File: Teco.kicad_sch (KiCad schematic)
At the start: 56 parts, among them Q1 BC848, Q2 BC848, Q3 IRLML9303, SW1 BUTTON

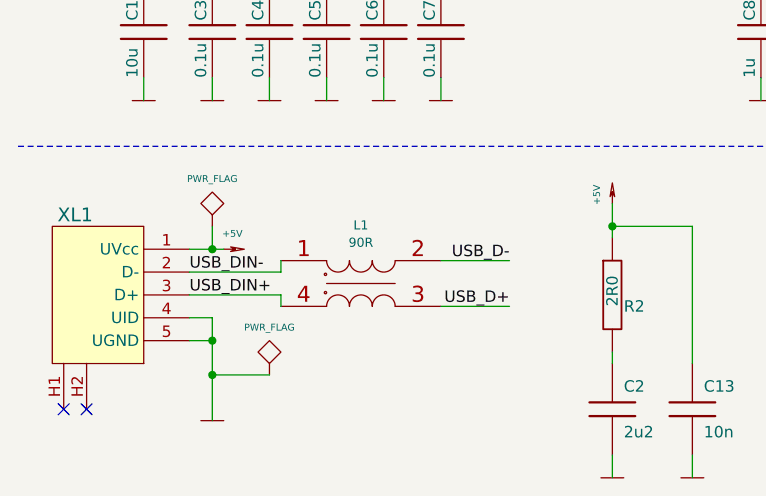
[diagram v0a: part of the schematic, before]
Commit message: switch to KiCAD 7
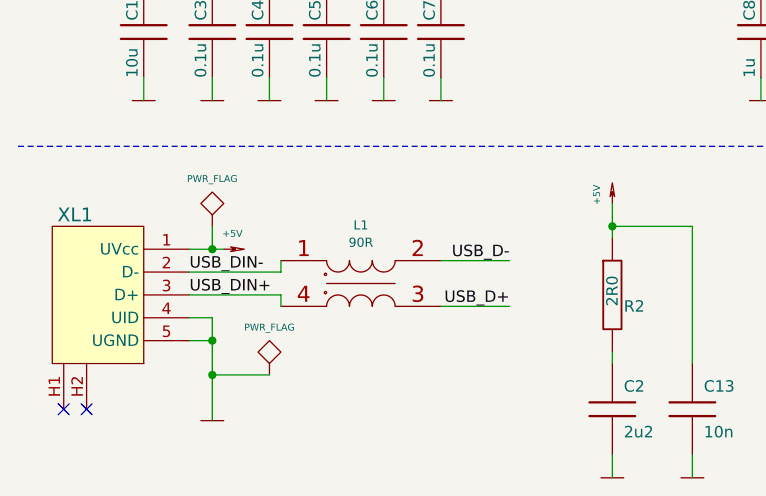
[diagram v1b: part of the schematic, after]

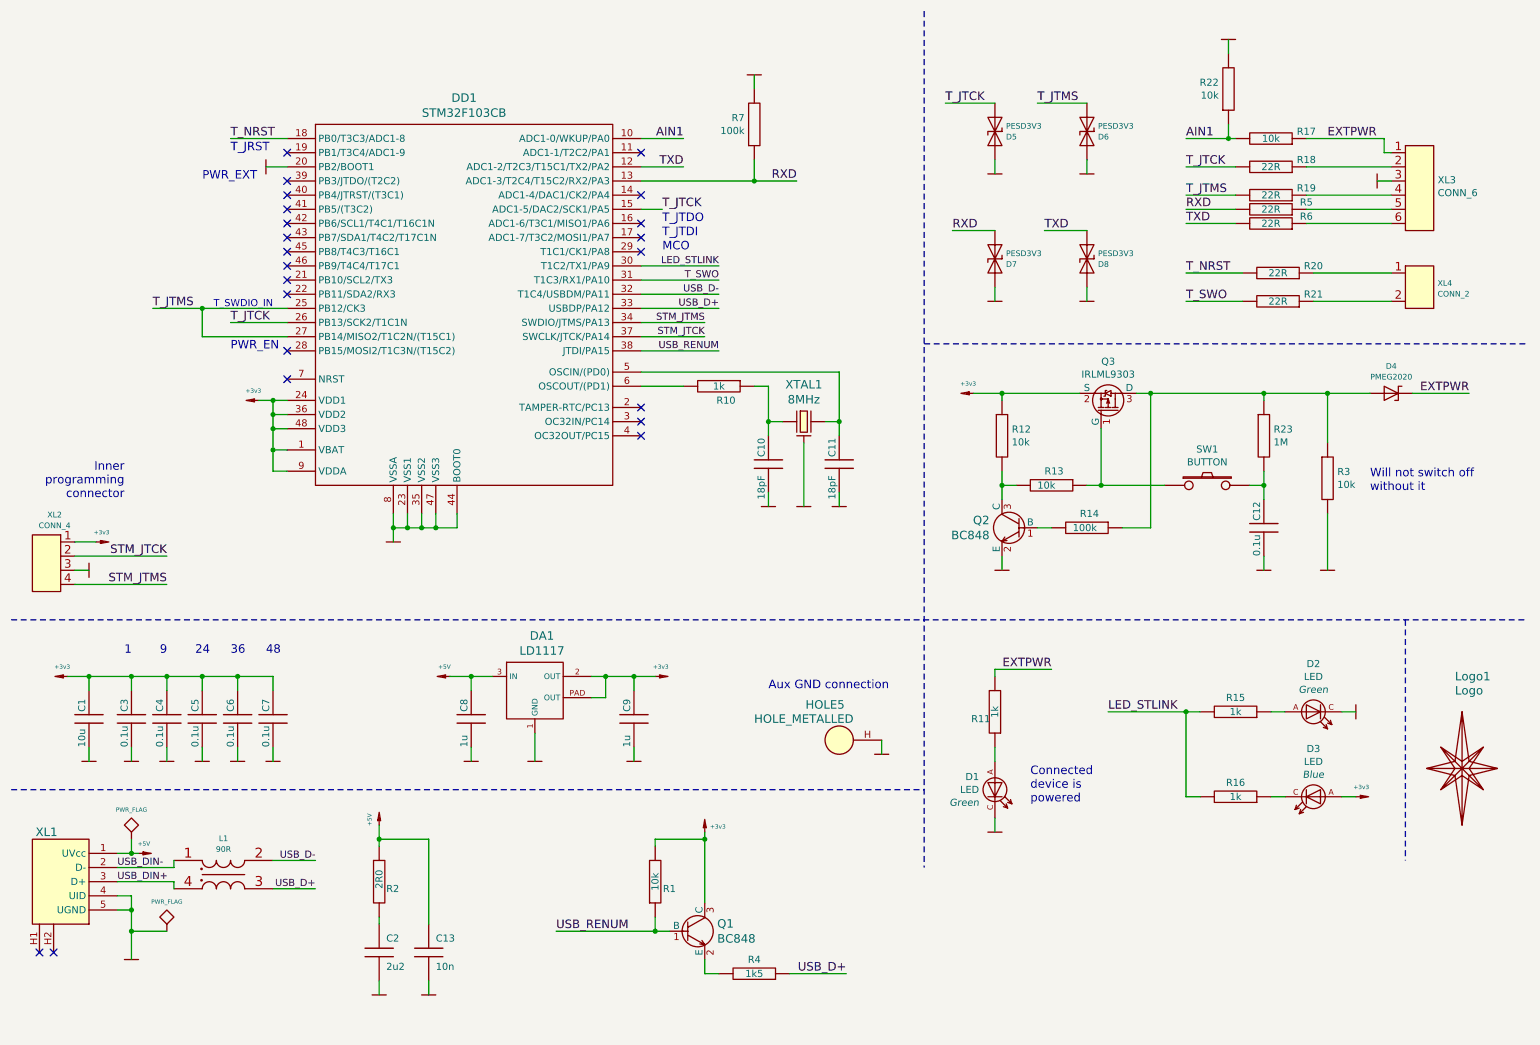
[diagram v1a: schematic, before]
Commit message: USB-C connector installed, ESD USB protection added, new BOM created
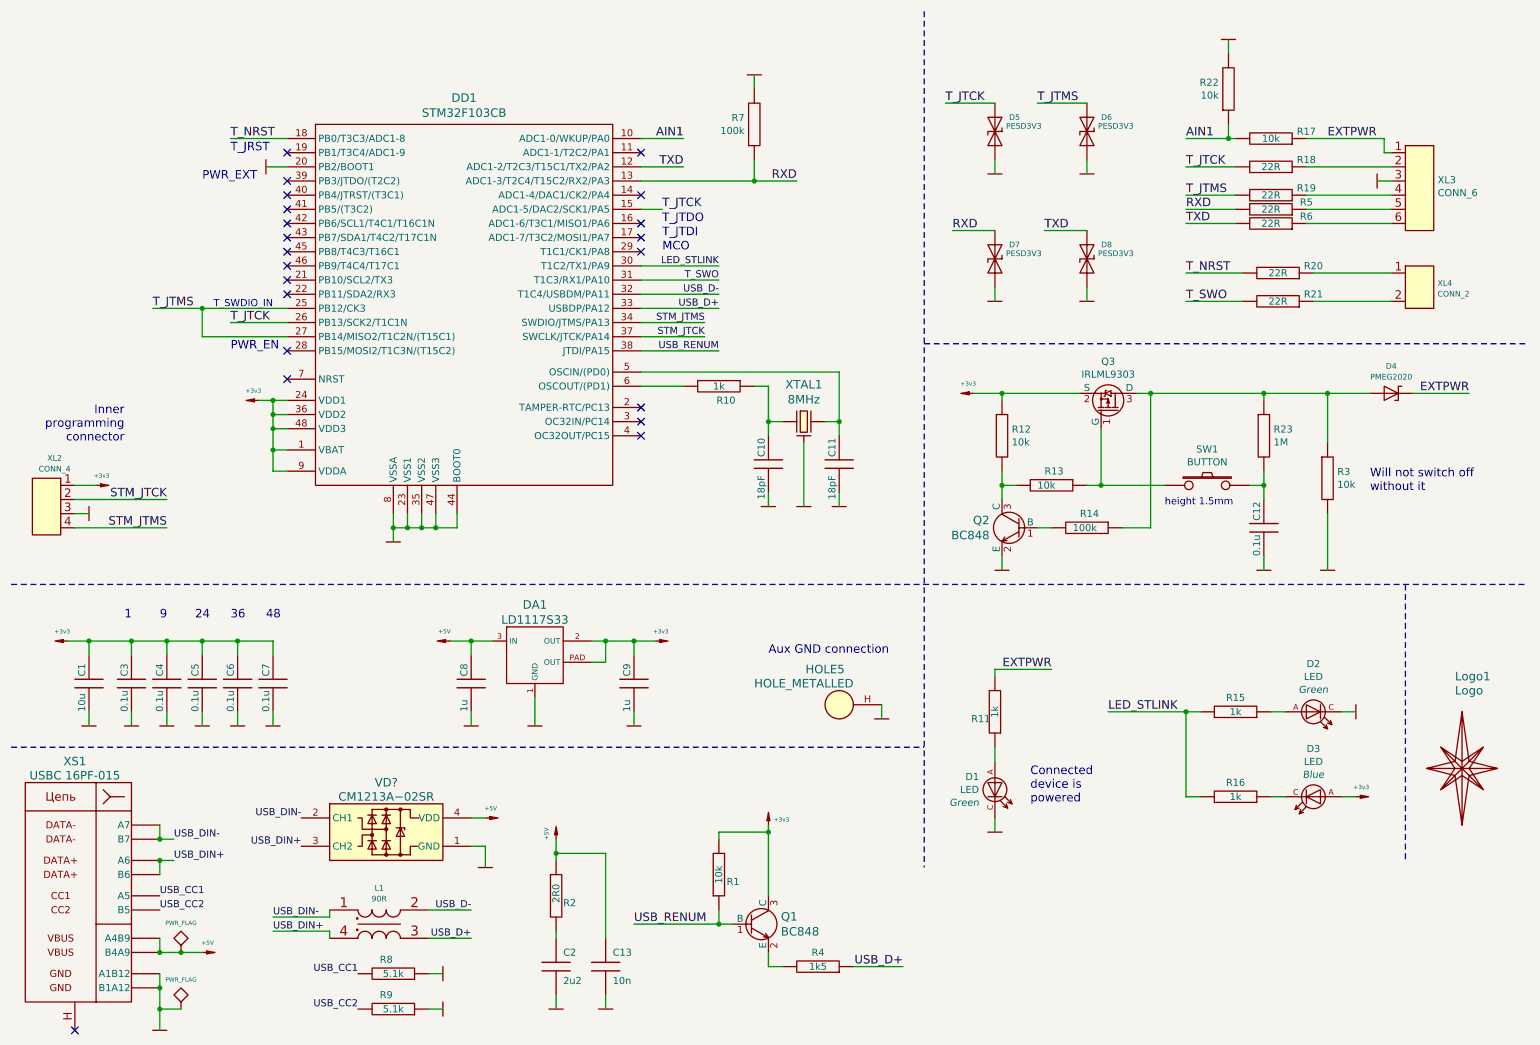
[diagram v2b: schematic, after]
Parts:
- removed XL1: USB_MICRO_2H, Connectors:USBmicro_MOLEX_1050170001, symbol Connectors_kl:USB_MICRO_2H
- added R8, R9: 5.1k, Resistors:RES0603, symbol Tittar_kl:R
- added VD?: CM1213A−02SR, SOT,_TO:SOT143, symbol Protection:CM1213A−02SR
- added XS1: USBC 16PF-015, Connectors:USB-C_16pin_16PF-015, symbol Connectors:USB-C_16pin
- DA1: value LD1117 -> LD1117S33
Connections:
- net +5v: now also VD?.4 (VDD), XS1.A4B9, XS1.B4A9
- net GND: now also R8.1, R9.1, VD?.1 (GND), XS1.A1B12, XS1.A8 (SBU1), XS1.B1A12
- net USB_DIN+: now also VD?.3 (CH2), XS1.A6, XS1.B6
- net USB_DIN-: now also VD?.2 (CH1), XS1.A7, XS1.B7
- new net USB_CC1: R8.2, XS1.A5
- new net USB_CC2: R9.2, XS1.B5
- no-connect marks 22 -> 21
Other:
- note added: "height 1.5mm"
- moved on the sheet: C1, C13, C2, C3, C4, C5, C6, C7, C8, C9, DA1, HOLE5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

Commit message: upgrade complete
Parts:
- D1, D2: value LED -> LED G
- D3: value LED -> LED B
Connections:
- net USB_DIN+: now also VD?.2 (CH1); no longer VD?.3 (CH2)
- net USB_DIN-: now also VD?.3 (CH2); no longer VD?.2 (CH1)
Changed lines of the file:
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@@
     (effects (font (size 1.524 1.524)) (justify left bottom))
   )
-  (label "USB_DIN-" (at 64.77 157.48 180) (fields_autoplaced)
+  (label "USB_DIN-" (at 64.77 162.56 180) (fields_autoplaced)
     (effects (font (size 1.27 1.27)) (justify right bottom))
   )
@@
     (effects (font (size 1.524 1.524)) (justify right bottom))
   )
-  (label "USB_DIN+" (at 64.77 162.56 180) (fields_autoplaced)
+  (label "USB_DIN+" (at 64.77 157.48 180) (fields_autoplaced)
     (effects (font (size 1.27 1.27)) (justify right bottom))
   )
@@
       (effects (font (size 1.27 1.27)) (justify left))
     )
-    (property "Value" "LED" (at 186.3852 152.4 90)
+    (property "Value" "LED G" (at 186.3852 152.4 90)
       (effects (font (size 1.27 1.27)) (justify left))
     )
@@
       (effects (font (size 1.27 1.27)))
     )
-    (property "Value" "LED" (at 246.38 132.1308 0)
+    (property "Value" "LED G" (at 246.38 132.1308 0)
       (effects (font (size 1.27 1.27)))
     )
@@
       (effects (font (size 1.27 1.27)))
     )
-    (property "Value" "LED" (at 246.38 147.3708 0)
-      (effects (font (size 1.27 1.27)))
-    )
+    (property "Value" "LED B" (at 246.38 147.3708 0)
+      (effects (font (size 1.27 1.27)))
+    )
